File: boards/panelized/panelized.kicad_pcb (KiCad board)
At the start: 2 copper layers, 99.7 x 99.1 mm, 128 parts, among them J1 RJ45, J2 RJ45, P1 CONN_2, P1 HE10-10, P2 CONN_7, Q1 IRLR110, Q1 NDS355, Q2 NDS355, Q3 NDS355, Q4 NDS355, Q5 NDS355, Q6 NDS355, Q7 NDS355, Q8 NDS355, SW1 SW_PUSH, U1 74HC595, U1 LM358, U2 SN74LVC1G74, U2 TS2937, U3 74HCT125, U4 TS2937

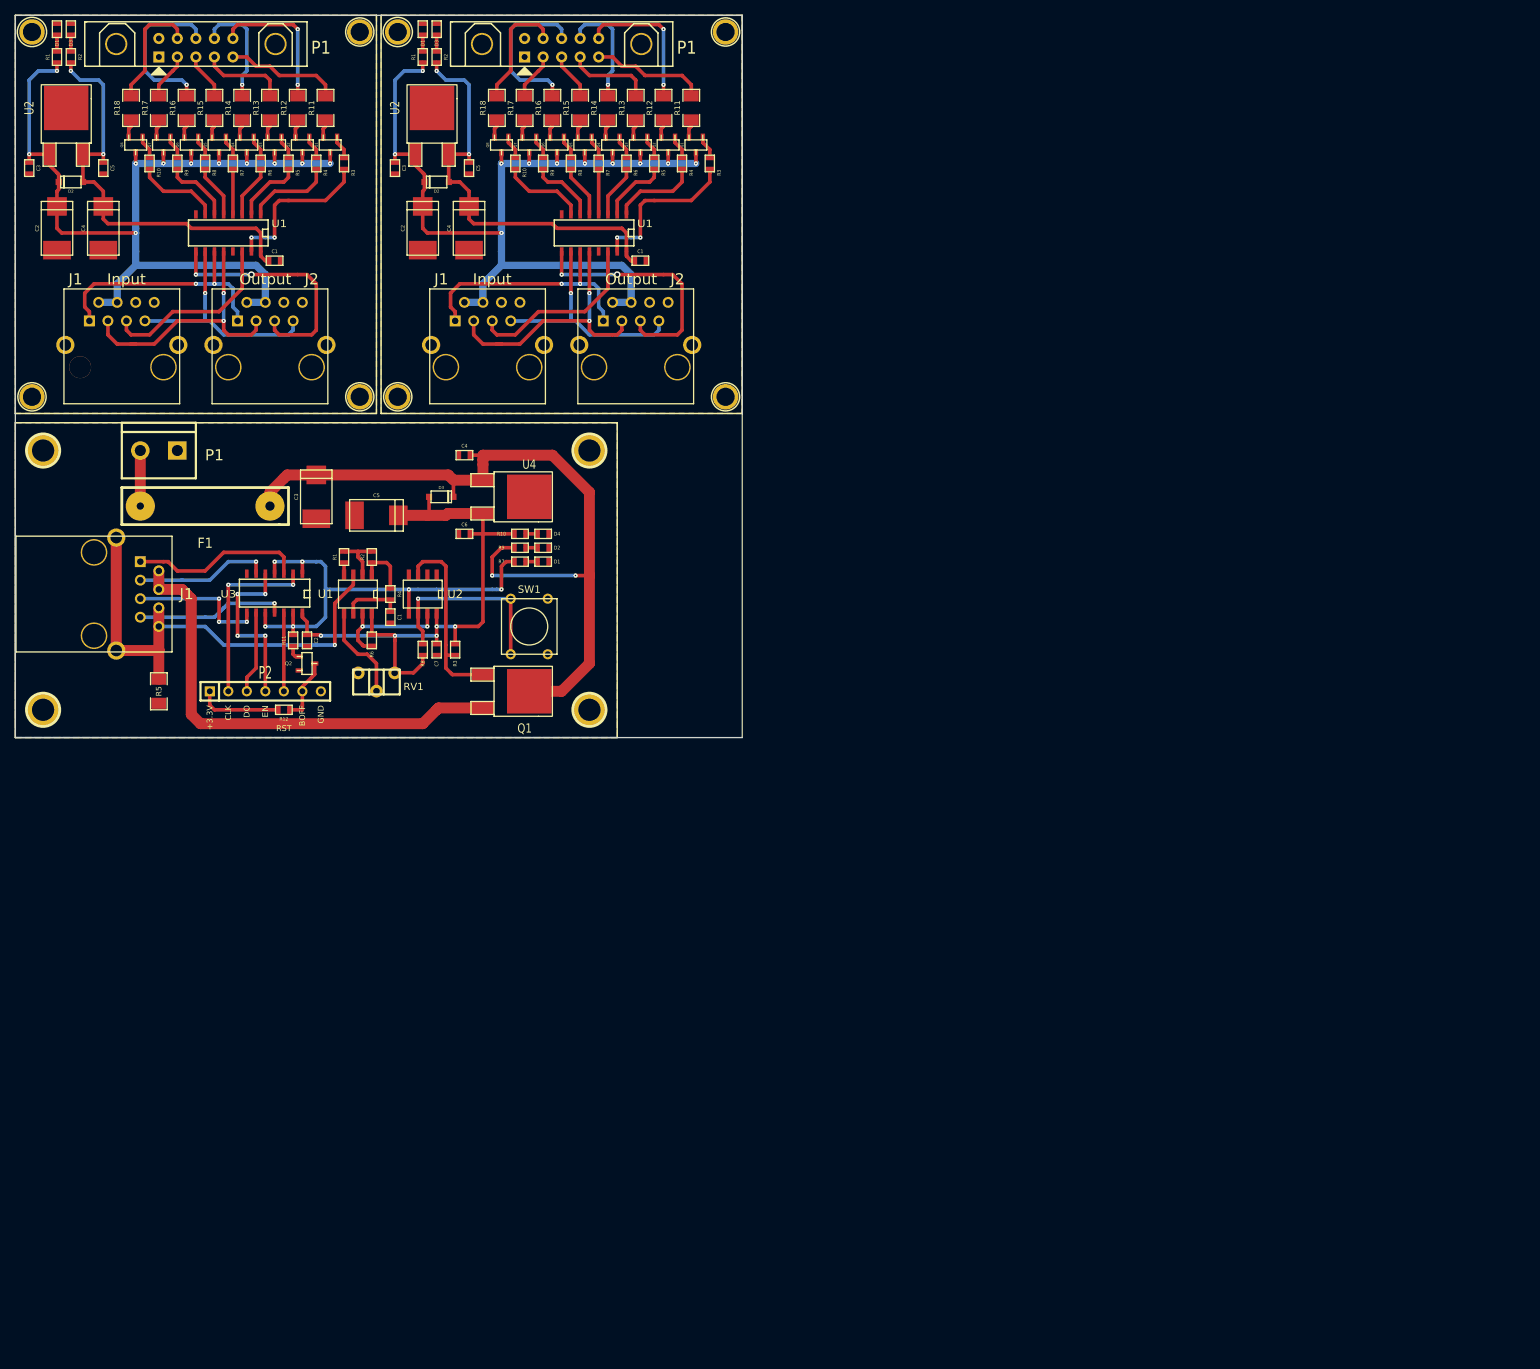
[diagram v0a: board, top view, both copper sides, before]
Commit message: Panelized boards
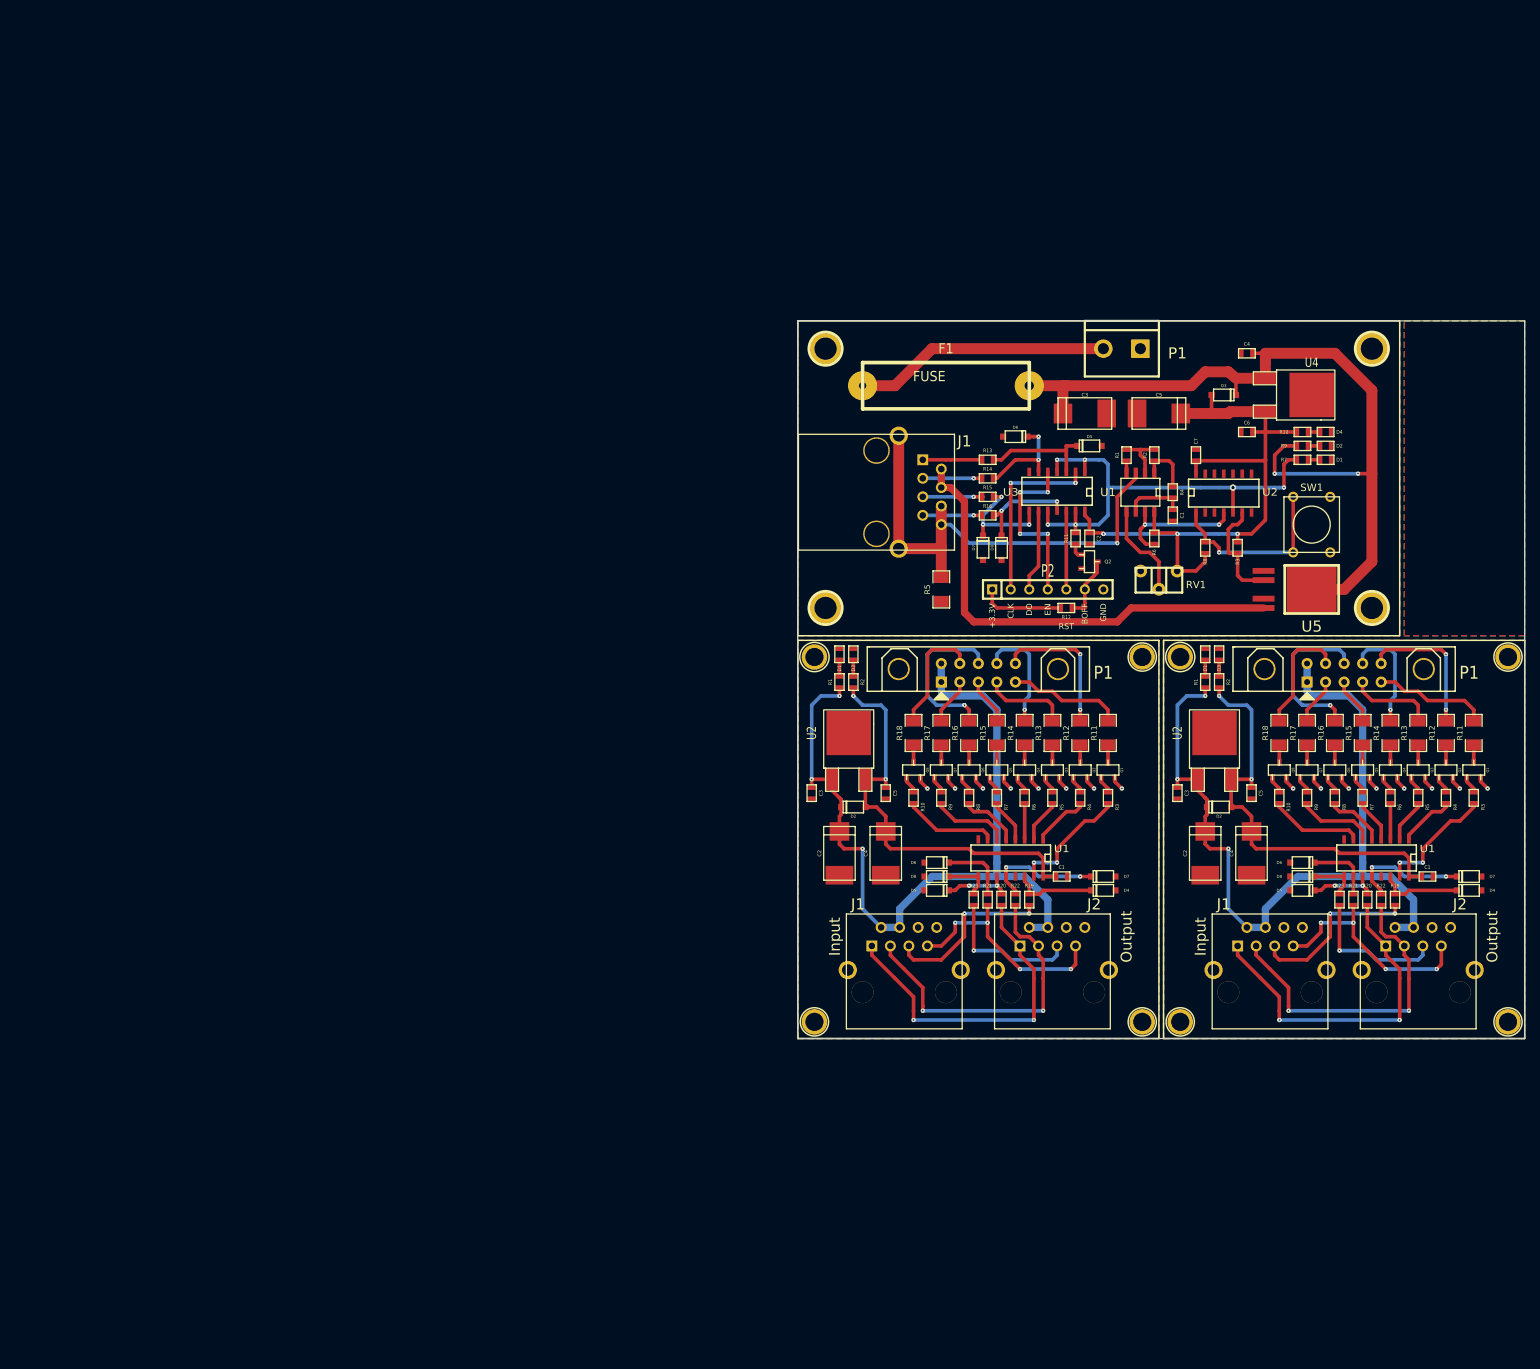
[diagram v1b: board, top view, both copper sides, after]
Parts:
- removed the 1PIN at (146.9, 36.6)
- removed the 1PIN at (146.9, 86.6)
- removed the 1PIN at (102.0, 86.6)
- removed the 1PIN at (102.0, 36.6)
- removed the J1 at (114.3, 82.5)
- removed the J1 at (64.1, 82.5)
- removed the J1 at (60.3, 113.7)
- removed the J2 at (134.6, 82.5)
- removed the J2 at (84.5, 82.5)
- removed the Q1 at (142.9, 52.1)
- removed the Q1 at (113.7, 127.0)
- removed the R10 at (118.1, 54.6)
- removed the R10 at (67.9, 54.6)
- removed the R13 at (134.6, 47.0)
- removed the R14 at (130.8, 47.0)
- removed the R15 at (127.0, 47.0)
- removed the R16 at (123.2, 47.0)
- added 1PIN: P***, 1pin, F.Cu at (254.3, 122.3)
- added 1PIN: P***, 1pin, F.Cu at (254.3, 172.3)
- added 1PIN: P***, 1pin, F.Cu at (209.3, 172.3)
- added 1PIN: P***, 1pin, F.Cu at (209.3, 122.3)
- added D4: ZENER, sod123, F.Cu at (248.9, 154.3)
- added D4: ZENER, sod123, F.Cu at (198.8, 154.3)
- added D5: ZENER, sod123, F.Cu at (226.1, 154.3)
- added D5: ZENER, sod123, F.Cu at (175.9, 154.3)
- added D5: ZENER_5.6V, sod123, F.Cu at (196.8, 93.3)
- added D6: ZENER, sod123, F.Cu at (226.1, 150.5)
- added D6: ZENER, sod123, F.Cu at (175.9, 150.5)
- added D6: ZENER_5.6V, sod123, F.Cu at (186.7, 92.1)
- added D7: ZENER, sod123, F.Cu at (248.9, 152.4)
- added D7: ZENER, sod123, F.Cu at (198.8, 152.4)
- added D7: ZENER_5.6V, sod123, F.Cu at (182.2, 107.3)
- added D8: ZENER, sod123, F.Cu at (226.1, 152.4)
- added D8: ZENER, sod123, F.Cu at (175.9, 152.4)
- added D8: ZENER_5.6V, sod123, F.Cu at (184.8, 107.3)
- added J1: RJ45, RJ45_MEBP_8-8G, F.Cu at (221.6, 168.3)
- added J1: RJ45, RJ45_MEBP_8-8G, F.Cu at (171.4, 168.3)
- added J1: RJ45, RJ45_MEBP_8-8G, F.Cu at (167.6, 99.7)
- added J2: RJ45, RJ45_MEBP_8-8G, F.Cu at (241.9, 168.3)
- added J2: RJ45, RJ45_MEBP_8-8G, F.Cu at (191.8, 168.3)
- added Q1: NDS355, sot23, F.Cu at (249.6, 137.8)
- added R10: 220, SM0603, F.Cu at (222.9, 141.6)
- added R10: 220, SM0603, F.Cu at (172.7, 141.6)
- added R13: 160, SM1206, F.Cu at (241.9, 132.7)
- added R13: 1k, SM0603, F.Cu at (182.9, 95.2)
- added R14: 160, SM1206, F.Cu at (238.1, 132.7)
- added R14: 1k, SM0603, F.Cu at (182.9, 97.8)
- added R15: 160, SM1206, F.Cu at (234.3, 132.7)
- added R15: 1k, SM0603, F.Cu at (182.9, 100.3)
- added R16: 160, SM1206, F.Cu at (230.5, 132.7)
- added R16: 1k, SM0603, F.Cu at (182.9, 102.9)
- added R19: 1k, SM0603, F.Cu at (238.8, 155.6)
- added R19: 1k, SM0603, F.Cu at (188.6, 155.6)
- added R20: 1k, SM0603, F.Cu at (234.9, 155.6)
- added R20: 1k, SM0603, F.Cu at (184.8, 155.6)
- added R21: 1k, SM0603, F.Cu at (233.0, 155.6)
- added R21: 1k, SM0603, F.Cu at (182.9, 155.6)
- added R22: 1k, SM0603, F.Cu at (236.9, 155.6)
- added R22: 1k, SM0603, F.Cu at (186.7, 155.6)
- added R23: 1k, SM0603, F.Cu at (231.1, 155.6)
- added R23: 1k, SM0603, F.Cu at (181.0, 155.6)
- added U5: BTS462, TO252-5L, F.Cu at (227.3, 113.0)
- C1: value 100n -> 100nF
- C2, C7: value 100nf -> 100nF
- F1: footprint fuse1 -> fuse22.5
- R3 (x2), R4 (x2), R5 (x2), R6 (x2), R7 (x2), R8 (x2), R9 (x2): value 200 -> 220
- U2: value SN74LVC1G74 -> 74HC74; footprint SO8E -> SO14E
- moved G*** 139.3 mm to (235.6, 138.4)
- moved G*** 139.3 mm to (185.4, 138.4)
- moved P1 137.4 mm to (231.8, 124.5)
- moved P1 137.4 mm to (181.6, 124.5)
- moved R12 137.4 mm to (195.6, 132.7)
- moved R13 137.4 mm to (191.8, 132.7)
- moved R14 137.4 mm to (188.0, 132.7)
- moved R15 137.4 mm to (184.2, 132.7)
- moved U1 137.4 mm to (186.1, 149.9)
- moved U2 137.4 mm to (163.8, 139.1)
- moved 1PIN 137.4 mm to (159.1, 122.3)
- moved 1PIN 137.4 mm to (159.1, 172.3)
- moved 1PIN 137.4 mm to (204.1, 172.3)
- moved 1PIN 137.4 mm to (204.1, 122.3)
- moved C2 137.4 mm to (212.7, 149.2)
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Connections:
- C1 pad 1: N-0000022 -> N-000002
- D2 pad 1: N-0000028 (its old number) -> N-0000032
- D4 pad 1: N-0000011 -> N-0000030
- F1 pad 1: N-0000010 -> N-0000029
- P1 pad 1: GND -> +24V (x2)
- P1 pad 2: GND -> +24V (x2)
- P1 pad 2: N-0000010 -> N-0000029
- Q1 pad 2: +24V -> N-0000022
- Q1 pad 3: N-0000011 -> GND
- Q2 pad 1: N-0000024 -> N-0000021 (x2)
- Q2 pad 2: +24V -> N-0000024 (x2)
- Q2 pad 3: N-0000022 -> GND (x2)
- Q2 pad 1: N-0000018 -> N-0000019
- Q3 pad 2: +24V -> N-0000019 (x2)
- Q3 pad 3: N-000003 -> GND (x2)
- Q4 pad 1: N-000001 -> N-0000018 (x2)
- Q4 pad 2: +24V -> N-0000017 (x2)
- Q4 pad 3: N-000005 -> GND (x2)
- Q5 pad 2: +24V -> N-0000025 (x2)
- Q5 pad 3: N-000007 (its old number) -> GND (x2)
- Q6 pad 2: +24V -> N-0000027 (x2)
- Q6 pad 3: N-0000010 -> GND (x2)
- Q7 pad 2: +24V -> N-0000036 (x2)
- Q7 pad 3: N-0000034 -> GND (x2)
- Q8 pad 2: +24V -> N-0000034 (x2)
- Q8 pad 3: N-0000037 (its old number) -> GND (x2)
- R1 pad 1: N-0000013 -> N-0000033
- R10 pad 2: N-0000011 -> N-0000030
- R11 pad 1: N-0000011 -> N-0000022 (x2)
- R11 pad 2: N-0000018 -> N-0000019
- R12 pad 1: N-0000022 -> N-0000024 (x2)
- R13 pad 1: N-000003 -> N-0000019
- R14 pad 1: N-000005 -> N-0000017
- R15 pad 1: N-000007 (its old number) -> N-0000025
- R16 pad 1: N-0000010 -> N-0000027
- R17 pad 1: N-0000034 -> N-0000036 (x2)
- R18 pad 1: N-0000037 (its old number) -> N-0000034 (x2)
- R2 pad 1: N-0000013 -> N-0000033
- R4 pad 1: N-0000024 -> N-0000021 (x2)
- R4 pad 2: N-0000022 -> N-000002
- R6 pad 1: N-000001 -> N-0000018 (x2)
- R8 pad 1: N-0000024 -> N-0000010
- R9 pad 2: N-0000028 (its old number) -> N-0000032
- RV1 pad 2: N-0000012 -> N-0000022
- SW1 pad 1: N-0000024 -> N-0000010
- U1 pad 10: Reset -> N-0000029 (x2)
- U1 pad 11: Clock -> N-0000030 (x2)
- U1 pad 12: Enable -> N-0000033 (x2)
- U1 pad 14: Data_In -> N-0000032 (x2)
- U1 pad 9: Data_Out -> N-0000031 (x2)
- U1 pad 2: N-0000013 -> N-0000033
- U1 pad 5: N-0000012 -> N-0000022
- U1 pad 6: N-0000022 -> N-000002
- U2 pad 1: GND -> N-0000010
- U2 pad 3: PowerOn -> GND
- U2 pad 4: GND -> Shutdown
- U2 pad 6: N-0000024 -> PowerOn
- U2 pad 7: Shutdown -> GND
- U2 pad 8: +5V -> (no net)
- U3 pad 11: Reset -> N-0000015
- U3 pad 3: Clock -> N-0000018
- U3 pad 6: Enable -> N-0000017
- U3 pad 8: Data_Out -> N-0000016
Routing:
- net N-0000031: track 0.00 -> 77.5 mm
- net N-0000027: track 65.2 -> 4.74 mm
- net N-0000029: track 0.00 -> 53.6 mm
- net N-0000033: track 0.00 -> 40.0 mm, vias 0 -> 4
- net Data_Out: track 87.2 -> 47.8 mm, vias 7 -> 3
- net GND: track 1.65 -> 31.7 mm, vias 0 -> 16
- net N-0000024: track 33.3 -> 4.74 mm, vias 1 -> 0
- net N-0000032: track 0.00 -> 24.4 mm
- net N-0000030: track 0.00 -> 20.7 mm, vias 0 -> 4
- net +24V: track 364.5 -> 344.1 mm, vias 24 -> 8
- net N-0000017: track 0.00 -> 18.3 mm, vias 0 -> 2
- net N-0000018: track 2.12 -> 20.4 mm
- net Reset: track 87.3 -> 70.8 mm, vias 3 -> 9
- net N-0000016: track 0.00 -> 15.8 mm, vias 0 -> 3
- net N-0000015: track 0.00 -> 14.2 mm, vias 0 -> 2
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- added copper zone on B.Cu, net (none)
- added copper zone on F.Cu, net (none)
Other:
- board size 99.7 x 99.1 mm -> 99.7 x 98.4 mm
- board text added: "Version 1.1"
- board text removed: "Version 1.0"

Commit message: Added logos
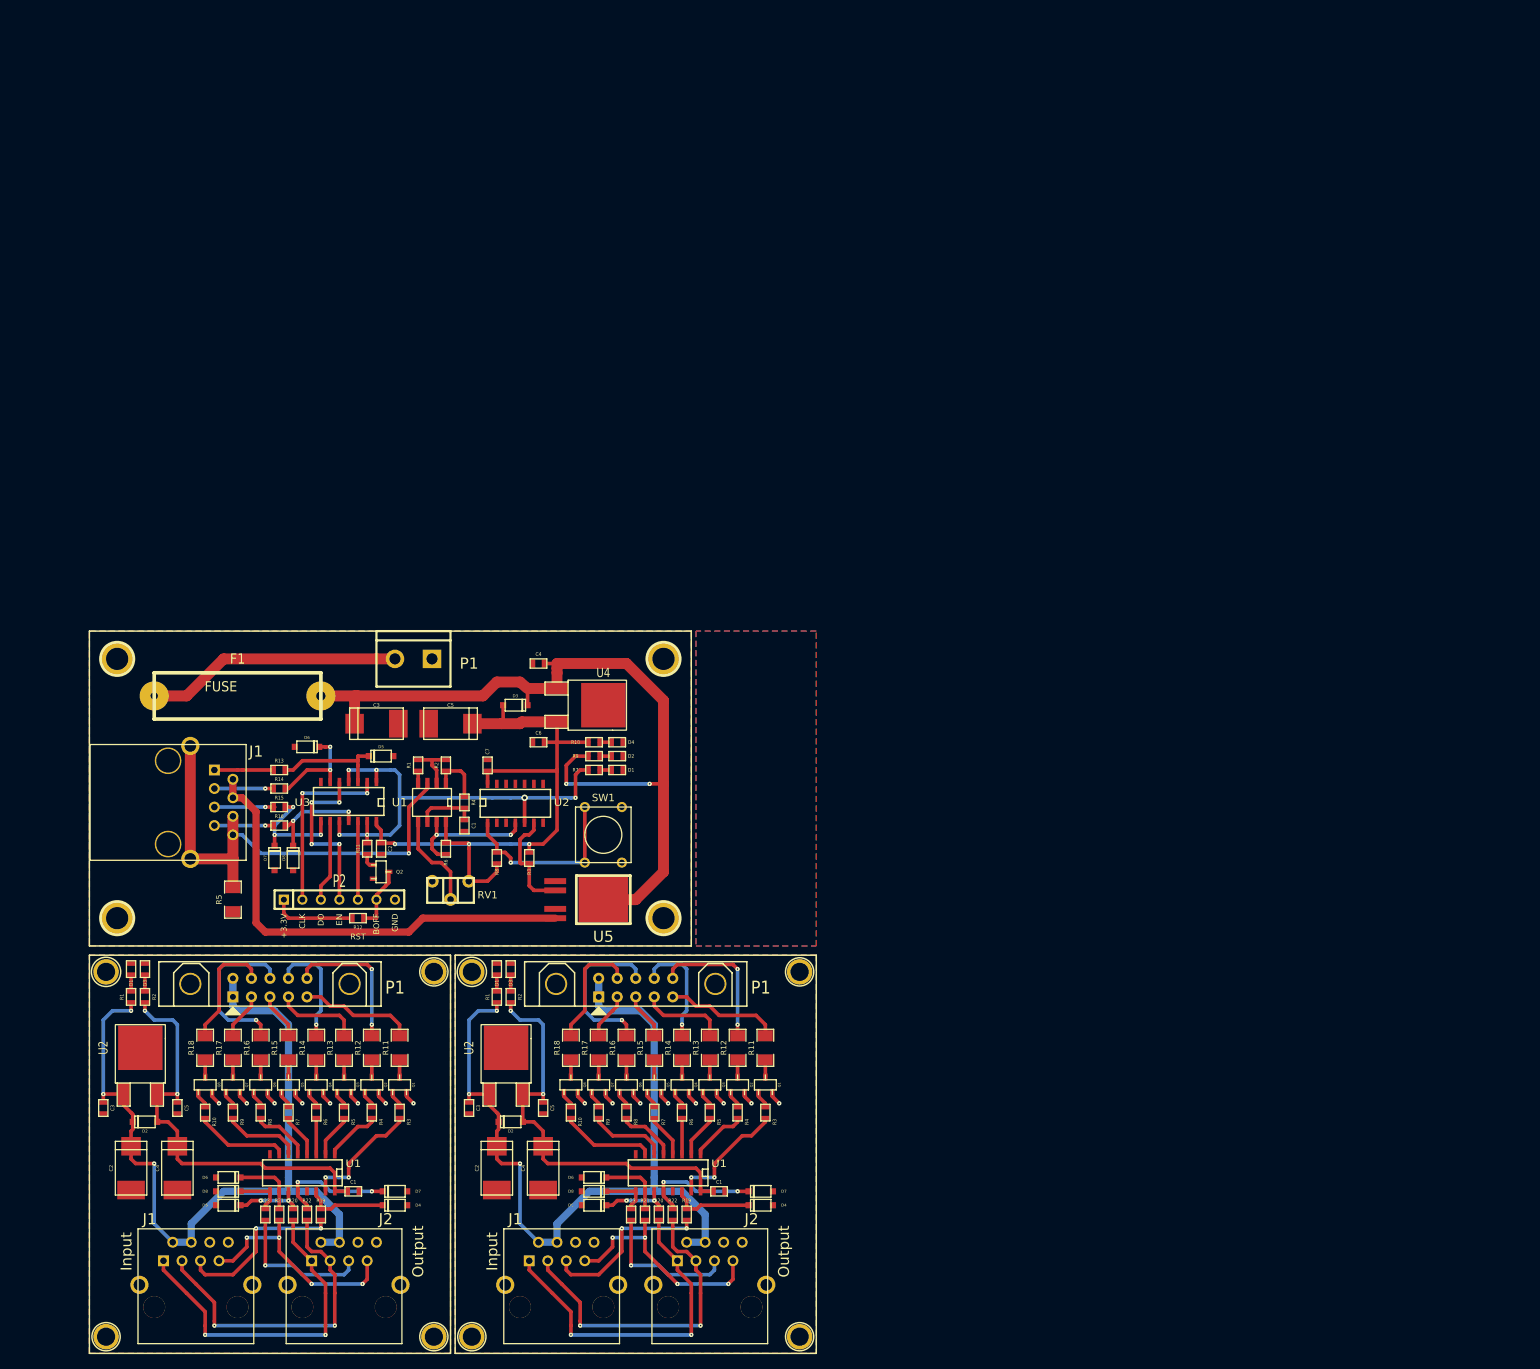
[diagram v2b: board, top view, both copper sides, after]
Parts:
- removed the 1PIN at (254.3, 122.3)
- removed the 1PIN at (254.3, 172.3)
- removed the 1PIN at (209.3, 172.3)
- removed the 1PIN at (209.3, 122.3)
- added 1PIN: P***, 1pin, F.Cu at (157.1, 165.5)
- added 1PIN: P***, 1pin, F.Cu at (157.1, 215.5)
- added 1PIN: P***, 1pin, F.Cu at (112.1, 215.5)
- added 1PIN: P***, 1pin, F.Cu at (112.1, 165.5)
- added G***: logo_hacker_silkbot_10_00mm, logo_hacker_silkbot_10_00mm, B.Cu at (123.8, 195.6)
- added G***: logo_hacker_silkbot_10_00mm, logo_hacker_silkbot_10_00mm, B.Cu at (73.7, 195.6)
- added G***: logo_hacker_silkbot_10_00mm, logo_hacker_silkbot_10_00mm, B.Cu at (79.4, 154.9)
- moved D5 106.3 mm to (78.7, 197.5)
- moved D6 106.3 mm to (78.7, 193.7)
- moved D8 106.3 mm to (78.7, 195.6)
- moved J1 106.3 mm to (124.5, 211.5)
- moved J2 106.3 mm to (94.6, 211.5)
- moved P1 106.3 mm to (84.5, 167.6)
- moved Q2 106.3 mm to (98.4, 181.0)
- moved Q3 106.3 mm to (94.6, 181.0)
- moved R12 106.3 mm to (98.4, 175.9)
- moved R13 106.3 mm to (94.6, 175.9)
- moved R4 106.3 mm to (98.4, 184.8)
- moved R5 106.3 mm to (94.6, 184.8)
- moved U2 106.3 mm to (66.7, 182.2)
- moved 1PIN 106.3 mm to (62.0, 165.5)
- moved 1PIN 106.3 mm to (62.0, 215.5)
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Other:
- board outline removed

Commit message: Fixed production files
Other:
- board outline added: 99.7 x 99.1 mm
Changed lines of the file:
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@@
     (area 59.337223 10.1575 233.0475 219.202)
     (thickness 1.6)
-    (drawings 53)
+    (drawings 51)
     (tracks 892)
     (zones 0)
@@
       (xy -0.14224 -2.76098) (xy -0.14224 -2.75336) (xy -0.14224 -2.74066) (xy -0.14224 -2.74066)) (layer B.SilkS) (width 0.00254))
   )
-  (gr_line (start 59.69 217.805) (end 159.385 217.805) (angle 90) (layer Eco2.User) (width 0.5))
-  (gr_line (start 59.69 118.745) (end 59.69 217.805) (angle 90) (layer Eco2.User) (width 0.5))
-  (gr_line (start 159.385 118.745) (end 59.69 118.745) (angle 90) (layer Eco2.User) (width 0.5))
-  (gr_line (start 159.385 217.805) (end 159.385 118.745) (angle 90) (layer Eco2.User) (width 0.5))
+  (gr_line (start 159.385 118.745) (end 59.69 118.745) (angle 90) (layer Edge.Cuts) (width 0.1))
+  (gr_line (start 159.385 217.805) (end 159.385 118.745) (angle 90) (layer Edge.Cuts) (width 0.1))
+  (gr_line (start 59.69 217.805) (end 159.385 217.805) (angle 90) (layer Edge.Cuts) (width 0.1))
+  (gr_line (start 59.69 118.745) (end 59.69 217.805) (angle 90) (layer Edge.Cuts) (width 0.1))
   (gr_text "7 segment led display driver" (at 137.033 186.563) (layer B.SilkS)
     (effects (font (size 1.5 1.5) (thickness 0.3)) (justify mirror))
@@
     (effects (font (size 0.8 0.8) (thickness 0.2)) (justify right))
   )
-  (target plus (at 233.045 10.16) (size 0.005) (width 0.1) (layer Edge.Cuts))
-  (target plus (at 233.045 10.16) (size 0.005) (width 0.1) (layer Edge.Cuts))
   (segment (start 121.285 202.565) (end 123.825 202.565) (width 1) (layer B.Cu) (net 1))
   (segment (start 141.605 202.565) (end 144.145 202.565) (width 1) (layer B.Cu) (net 1))
